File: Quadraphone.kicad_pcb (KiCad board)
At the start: 4 copper layers, 60 x 100 mm, 192 parts, among them J1 Conn_01x10_Male, J2 Conn_01x10_Male, J3 Conn_01x10_Male, J4 Conn_01x10_Male, J5 Eurorack_10_pin_power, U1 AMS1117-5.0, U10 TL072, U11 4066, U12 SSI2131, U13 TL072, U14 LM4040DBZ-2.5, U15 4066, U16 TL072, U17 SSI2131, U18 TL072, U22 SSI2131, U3 MCP6002, U4 LM4040DBZ-5, U5 MCP6004, U6 4066, U7 4066, U8 4066, U9 SSI2131

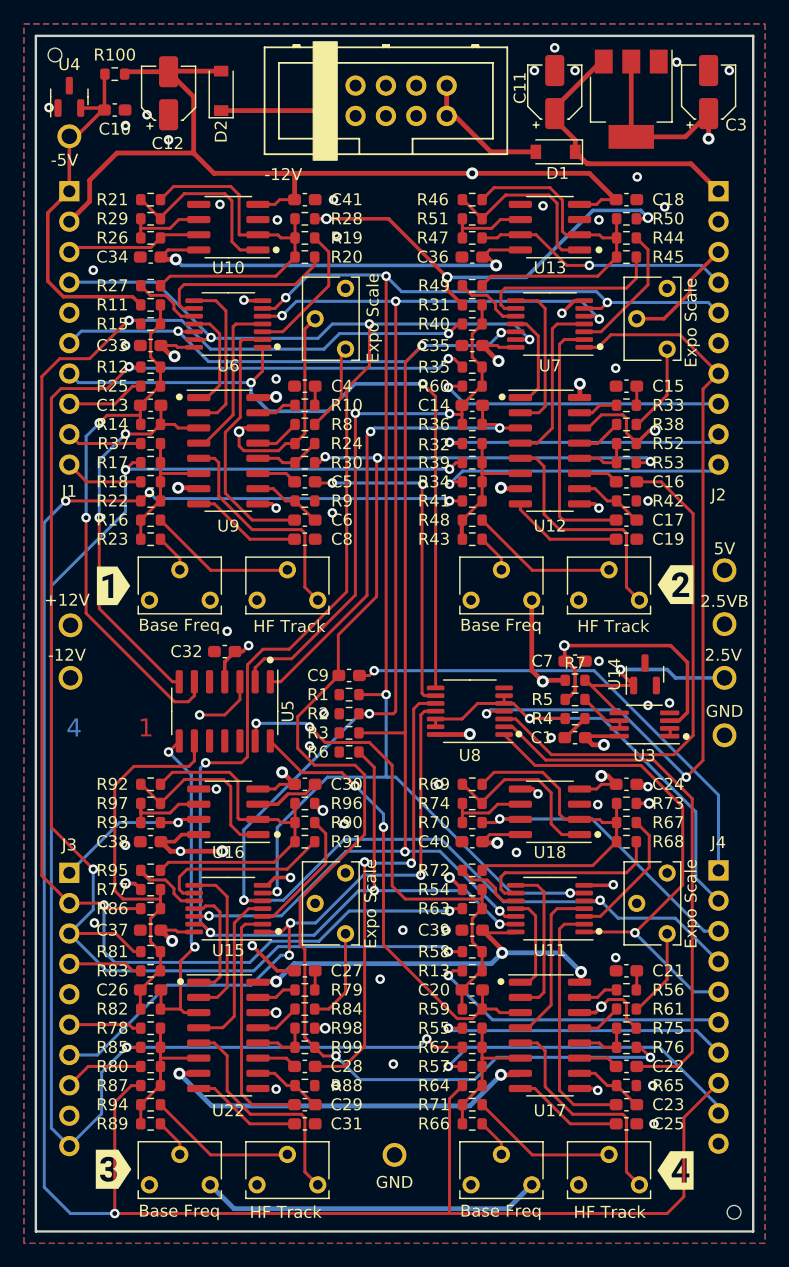
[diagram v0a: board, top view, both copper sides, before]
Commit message: v2.0 Update with Synch pulse at start to fix oscillators not starting
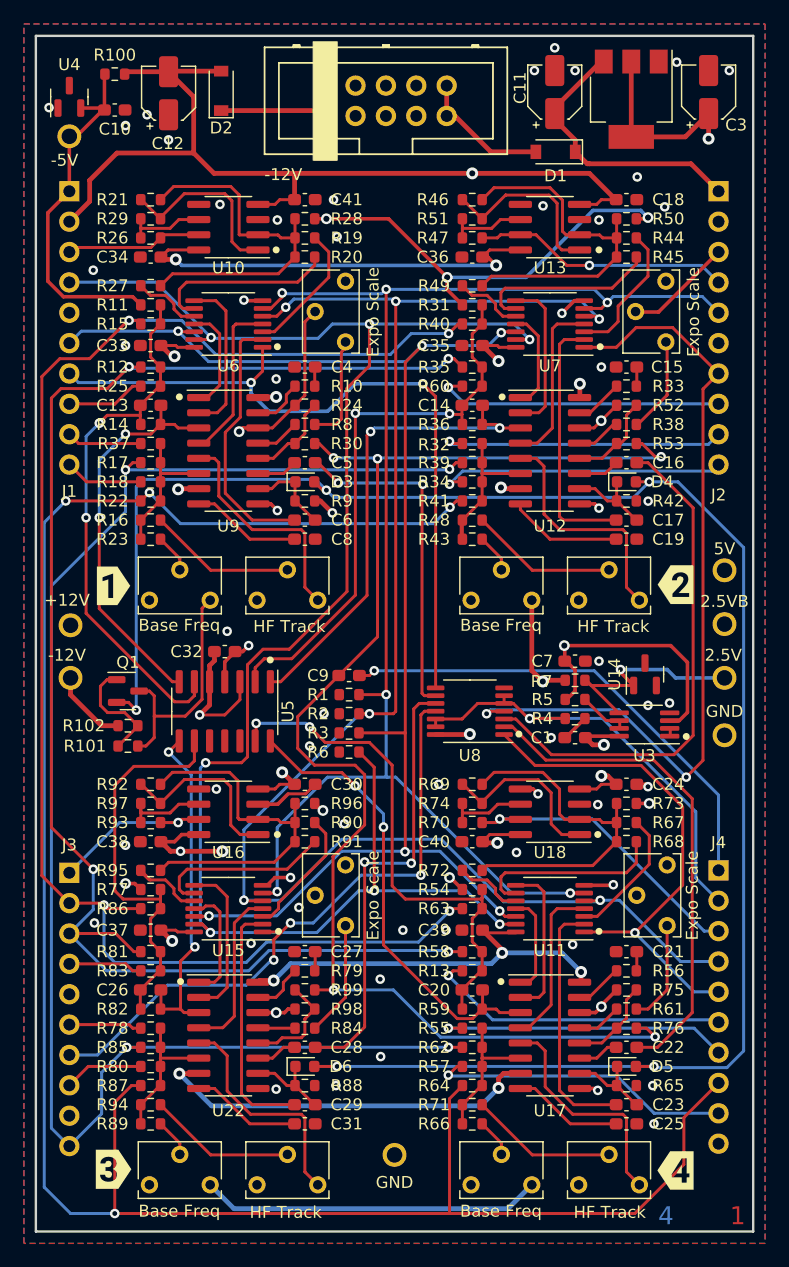
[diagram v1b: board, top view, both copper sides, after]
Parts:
- removed REF** (x2): JL_SMT_Assembly, Custom_Footprints:JLC_SMT_Tooling_Hole
- added D3: CDBU40, Diode_SMD:D_0603_1608Metric, F.Cu at (72.5, 87.3)
- added D4: CDBU40, Diode_SMD:D_0603_1608Metric, F.Cu at (99.4, 87.3)
- added D5: CDBU40, Diode_SMD:D_0603_1608Metric, F.Cu at (99.4, 136.2)
- added D6: CDBU40, Diode_SMD:D_0603_1608Metric, F.Cu at (72.5, 136.2)
- added Q1: MMBT3904, Package_TO_SOT_SMD:SOT-23, F.Cu at (57.7, 104.8)
- added R101: 20k, Resistor_SMD:R_0603_1608Metric, F.Cu at (57.7, 109.4)
- added R102: 47k, Resistor_SMD:R_0603_1608Metric, F.Cu at (57.7, 107.7)
- R17, R39, R62, R85: value 100k -> 680k
- R22, R41, R64, R87: value 49.9k -> 68k
- U11, U15, U6, U7, U8: value 4066 -> 74LV4066PW
- moved FID1 64.1 mm to (105.7, 148.7)
- moved R99 4.80 mm to (72.5, 129.8)
- moved R24 3.20 mm to (72.5, 80.9)
- moved R52 3.20 mm to (99.4, 80.9), turned to 180 degrees
- moved R75 3.20 mm to (99.4, 129.8), turned to 180 degrees
- moved R56 1.60 mm to (99.4, 128.2)
- moved R79 1.60 mm to (72.5, 128.2)
- moved R10 1.60 mm to (72.5, 79.3)
- moved R30 1.60 mm to (72.5, 84.1)
- moved R33 1.60 mm to (99.4, 79.3)
- moved R53 1.60 mm to (99.4, 84.1)
- moved C15 1.60 mm to (99.4, 77.7)
- moved C16 1.60 mm to (99.4, 85.7)
- moved C21 1.60 mm to (99.4, 126.6)
- moved C22 1.60 mm to (99.4, 134.6)
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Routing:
- net /Start_Pulse: track 0.00 -> 157.7 mm, vias 0 -> 5
- net +5V: track 317.5 -> 337.1 mm
- net +2V5: track 304.9 -> 294.8 mm, vias 7 -> 6
- net Net-(Q1-Pad1): track 0.00 -> 9.40 mm
- net -12V: track 277.7 -> 284.7 mm
- net /OSCVoice3/Linear_Frequency: track 4.85 -> 8.98 mm
- net /Linear_Frequency: track 120.1 -> 116.4 mm
- net GND: track 34.3 -> 37.8 mm, vias 57 -> 58
- net /OSCVoice2/Linear_Frequency: track 4.85 -> 7.70 mm
- net /OSCVoice4/Linear_Frequency: track 4.85 -> 7.50 mm
- net /OSCVoice4/Soft_Synch: track 44.6 -> 42.0 mm
- net /OSCVoice1/Linear_Frequency: track 5.56 -> 7.50 mm
- net /FREQ_MOD4: track 27.1 -> 25.4 mm
- net Net-(C29-Pad1): track 5.87 -> 7.49 mm
- net Net-(C23-Pad1): track 5.87 -> 7.49 mm
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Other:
- board text added: "Quadraphone Components v2.0 Mountjoy Modular"
- board text removed: "Quadraphone Components v1.0 Mountjoy Modular"

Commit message: Completed layout of synch pulse modification
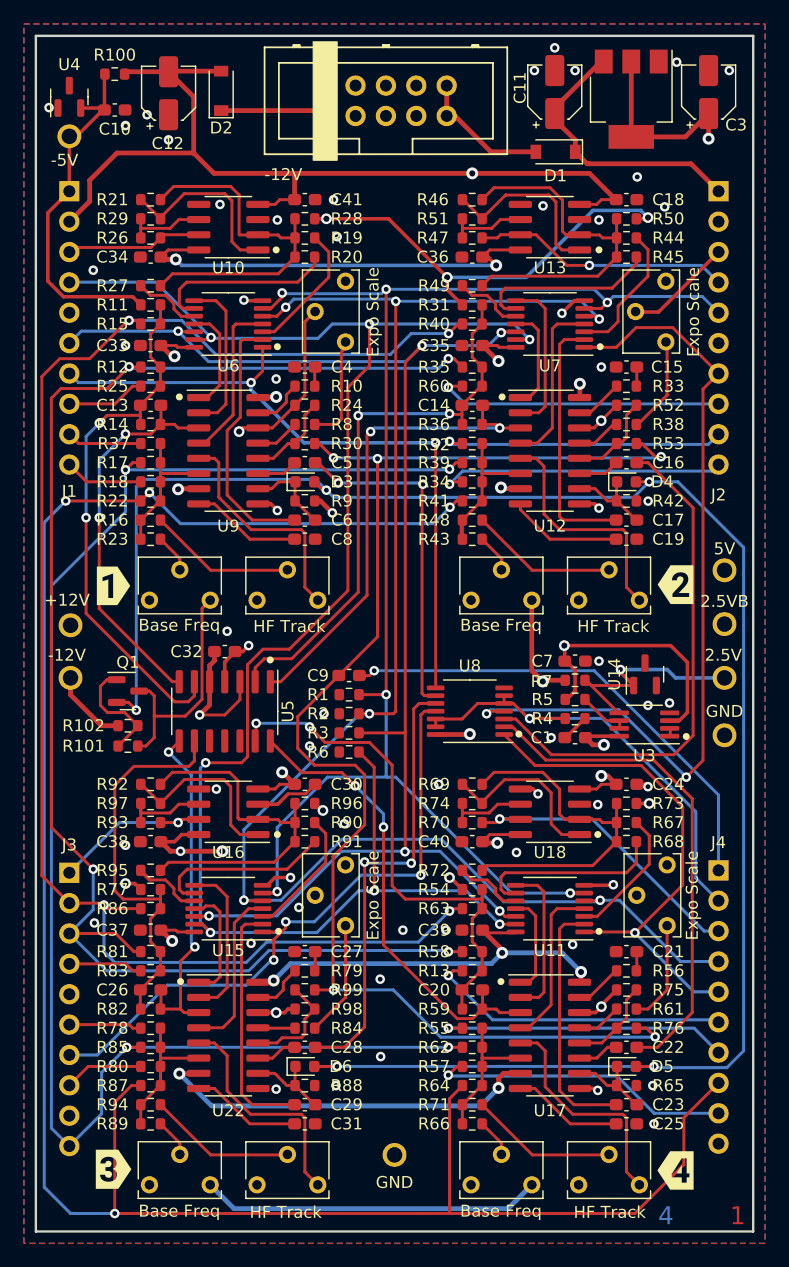
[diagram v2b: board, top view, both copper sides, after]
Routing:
- net /SYNCH_SIGNAL1: track 61.6 -> 57.2 mm

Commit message: Added alternative control pcb layout with 3 way switch for octave
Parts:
- R23, R43, R66, R89: value 49.9k -> 100k
